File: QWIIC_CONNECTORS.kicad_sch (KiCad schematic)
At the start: 6 parts, among them J20 Conn_01x04_Female, J21 Conn_01x04_Female, J22 Conn_01x04_Female, J23 Conn_01x04_Female, J24 Conn_01x04_Female, J25 Conn_01x04_Female

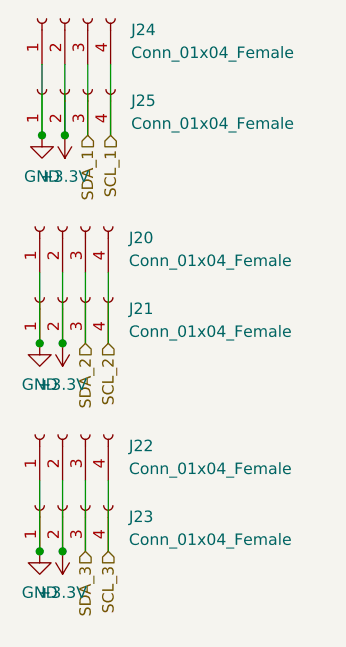
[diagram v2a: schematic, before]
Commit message: Added usb to ethernet and changed mcu to stm32g4
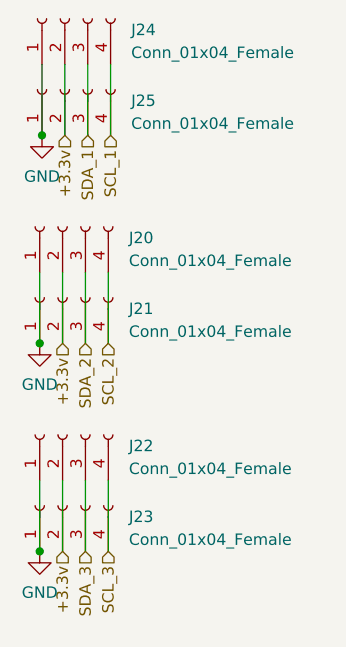
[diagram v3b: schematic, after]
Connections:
- net +3V3 renamed +3.3v
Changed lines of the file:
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@@
 (kicad_sch (version 20210621) (generator eeschema)
   (paper "A4")
-  (junction (at 53.34 107.696) (diameter 0) (color 0 0 0 0))
   (junction (at 50.8 84.582) (diameter 0) (color 0 0 0 0))
   (junction (at 51.054 61.468) (diameter 0) (color 0 0 0 0))
-  (junction (at 53.594 61.468) (diameter 0) (color 0 0 0 0))
   (junction (at 50.8 107.696) (diameter 0) (color 0 0 0 0))
-  (junction (at 53.34 84.582) (diameter 0) (color 0 0 0 0))
   (wire (pts (xy 50.8 99.822) (xy 50.8 107.696))
     (stroke (width 0) (type default) (color 0 0 0 0))
@@
     (effects (font (size 1.27 1.27)) (justify right))
   )
+  (hierarchical_label "+3.3v" (shape input) (at 53.594 61.468 270)
+    (effects (font (size 1.27 1.27)) (justify right))
+  )
   (hierarchical_label "SCL_1" (shape input) (at 58.674 61.468 270)
     (effects (font (size 1.27 1.27)) (justify right))
@@
   )
   (hierarchical_label "SCL_2" (shape input) (at 58.42 84.582 270)
+    (effects (font (size 1.27 1.27)) (justify right))
+  )
+  (hierarchical_label "+3.3v" (shape input) (at 53.34 107.696 270)
+    (effects (font (size 1.27 1.27)) (justify right))
+  )
+  (hierarchical_label "+3.3v" (shape input) (at 53.34 84.582 270)
     (effects (font (size 1.27 1.27)) (justify right))
   )
@@
     (pin "4")
   )
-  (symbol (lib_id "power:+3.3V") (at 53.34 107.696 180) (unit 1)
-    (in_bom yes) (on_board yes) (fields_autoplaced)
-    (property "Reference" "#PWR080" (id 0) (at 53.34 103.886 0)
-      (effects (font (size 1.27 1.27)) hide)
-    )
-    (property "Value" "+3.3V" (id 1) (at 53.34 112.268 0))
-    (property "Footprint" "" (id 2) (at 53.34 107.696 0)
-      (effects (font (size 1.27 1.27)) hide)
-    )
-    (property "Datasheet" "" (id 3) (at 53.34 107.696 0)
-      (effects (font (size 1.27 1.27)) hide)
-    )
-    (pin "1")
-  )
   (symbol (lib_id "Connector:Conn_01x04_Female") (at 53.594 48.514 90) (unit 1)
     (in_bom yes) (on_board yes) (fields_autoplaced)
@@
     (pin "4")
   )
-  (symbol (lib_id "power:+3.3V") (at 53.594 61.468 180) (unit 1)
-    (in_bom yes) (on_board yes) (fields_autoplaced)
-    (property "Reference" "#PWR081" (id 0) (at 53.594 57.658 0)
-      (effects (font (size 1.27 1.27)) hide)
-    )
-    (property "Value" "+3.3V" (id 1) (at 53.594 66.04 0))
-    (property "Footprint" "" (id 2) (at 53.594 61.468 0)
-      (effects (font (size 1.27 1.27)) hide)
-    )
-    (property "Datasheet" "" (id 3) (at 53.594 61.468 0)
-      (effects (font (size 1.27 1.27)) hide)
-    )
-    (pin "1")
-  )
   (symbol (lib_id "power:GND") (at 50.8 84.582 0) (unit 1)
     (in_bom yes) (on_board yes) (fields_autoplaced)
@@
     (pin "4")
   )
-  (symbol (lib_id "power:+3.3V") (at 53.34 84.582 180) (unit 1)
-    (in_bom yes) (on_board yes) (fields_autoplaced)
-    (property "Reference" "#PWR079" (id 0) (at 53.34 80.772 0)
-      (effects (font (size 1.27 1.27)) hide)
-    )
-    (property "Value" "+3.3V" (id 1) (at 53.34 89.154 0))
-    (property "Footprint" "" (id 2) (at 53.34 84.582 0)
-      (effects (font (size 1.27 1.27)) hide)
-    )
-    (property "Datasheet" "" (id 3) (at 53.34 84.582 0)
-      (effects (font (size 1.27 1.27)) hide)
-    )
-    (pin "1")
-  )
   (symbol (lib_id "Connector:Conn_01x04_Female") (at 53.34 79.502 90) (unit 1)
